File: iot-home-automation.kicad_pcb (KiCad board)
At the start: 4 copper layers, 53.2 x 41.6 mm, 25 parts, among them J1 Conn_01x05_Pin, J2 Conn_01x08_Pin, J3 Conn_01x02_Pin, J4 Conn_02x08_Odd_Even, J6 Conn_01x02_Pin, Q1 PMOS, SW1 SW_Push_SPDT, U1 STM32WB5MMGH6TR, U2 SHTC3, U3 AP2127K-1.8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

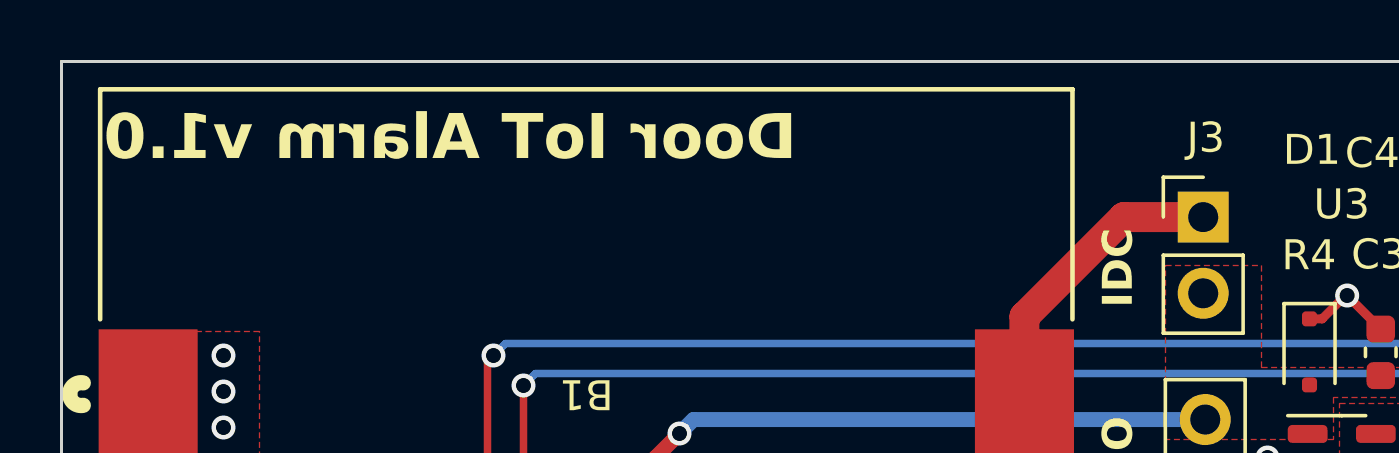
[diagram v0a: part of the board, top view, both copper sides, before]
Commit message: Silkscreen errata
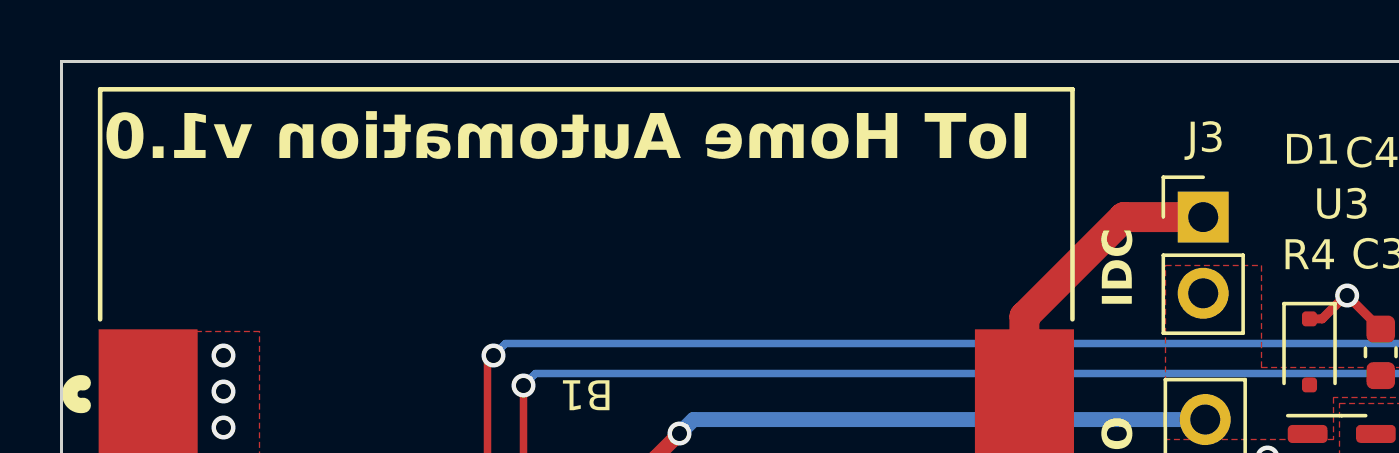
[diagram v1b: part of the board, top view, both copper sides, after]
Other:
- board text added: "IoT Home Automation v1.0"
- board text removed: "Door IoT Alarm v1.0"
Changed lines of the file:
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@@
     (effects (font (size 1 1) (thickness 0.2) bold) (justify left bottom))
   )
-  (gr_text "Door IoT Alarm v1.0" (at 120.2 86.4) (layer "F.SilkS")
+  (gr_text "IoT Home Automation v1.0" (at 120.2 86.4) (layer "F.SilkS")
     (effects (font (size 1.5 1.5) (thickness 0.25) bold) (justify right bottom mirror))
   )
